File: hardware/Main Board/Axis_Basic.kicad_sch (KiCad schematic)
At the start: 58 parts, among them J1 USB_C_Receptacle_USB2.0, J2 JST_PH, J3 JST_PH, J4 S2B-PH-K-S, J5 1175-1628-ND, J6 1-84952-4, SW1 RKB2SJK, SW2 RKB2SJK, U1 TLV493D, U2 UA78M33CDCYR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

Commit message: PCB ordered
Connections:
- net AUX1: now reaches J6.5 (Pin_5)
- net AUX1: now also U3.15 (PA10/SERCOM0_2/SERCOM2_2)
- net AUX2: now reaches J6.6 (Pin_6)
- net AUX2: now also U3.28 (PA19/SERCOM1_3/SERCOM3_3)
- no-connect marks 11 -> 10
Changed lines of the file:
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@@
   (no_connect (at 40.64 54.61))
   (no_connect (at 139.7 39.37))
-  (no_connect (at 90.17 128.27))
   (no_connect (at 33.02 110.49))
   (no_connect (at 196.85 139.7))
@@
     )
   )
+  (global_label "AUX2" (shape input) (at 133.35 114.3 0) (fields_autoplaced)
+    (effects (font (size 1.27 1.27)) (justify left))
+    (property "Intersheetrefs" "${INTERSHEET_REFS}" (at 141.1733 114.3 0)
+      (effects (font (size 1.27 1.27)) (justify left) hide)
+    )
+  )
   (global_label "MOTOR_B2" (shape input) (at 237.49 121.92 0) (fields_autoplaced)
     (effects (font (size 1.27 1.27)) (justify left))
@@
     )
   )
+  (global_label "AUX2" (shape input) (at 63.5 115.57 0) (fields_autoplaced)
+    (effects (font (size 1.27 1.27)) (justify left))
+    (property "Intersheetrefs" "${INTERSHEET_REFS}" (at 71.3233 115.57 0)
+      (effects (font (size 1.27 1.27)) (justify left) hide)
+    )
+  )
   (global_label "EN" (shape input) (at 196.85 101.6 180) (fields_autoplaced)
     (effects (font (size 1.27 1.27)) (justify right))
@@
     )
   )
+  (global_label "AUX1" (shape input) (at 90.17 128.27 180) (fields_autoplaced)
+    (effects (font (size 1.27 1.27)) (justify right))
+    (property "Intersheetrefs" "${INTERSHEET_REFS}" (at 82.3467 128.27 0)
+      (effects (font (size 1.27 1.27)) (justify right) hide)
+    )
+  )
   (global_label "DIR" (shape input) (at 133.35 132.08 0) (fields_autoplaced)
     (effects (font (size 1.27 1.27)) (justify left))
@@
       (effects (font (size 1.27 1.27)) (justify left) hide)
     )
+  )
+  (global_label "AUX1" (shape input) (at 63.5 118.11 0) (fields_autoplaced)
+    (effects (font (size 1.27 1.27)) (justify left))
+    (property "Intersheetrefs" "${INTERSHEET_REFS}" (at 71.3233 118.11 0)
+      (effects (font (size 1.27 1.27)) (justify left) hide)
+    )

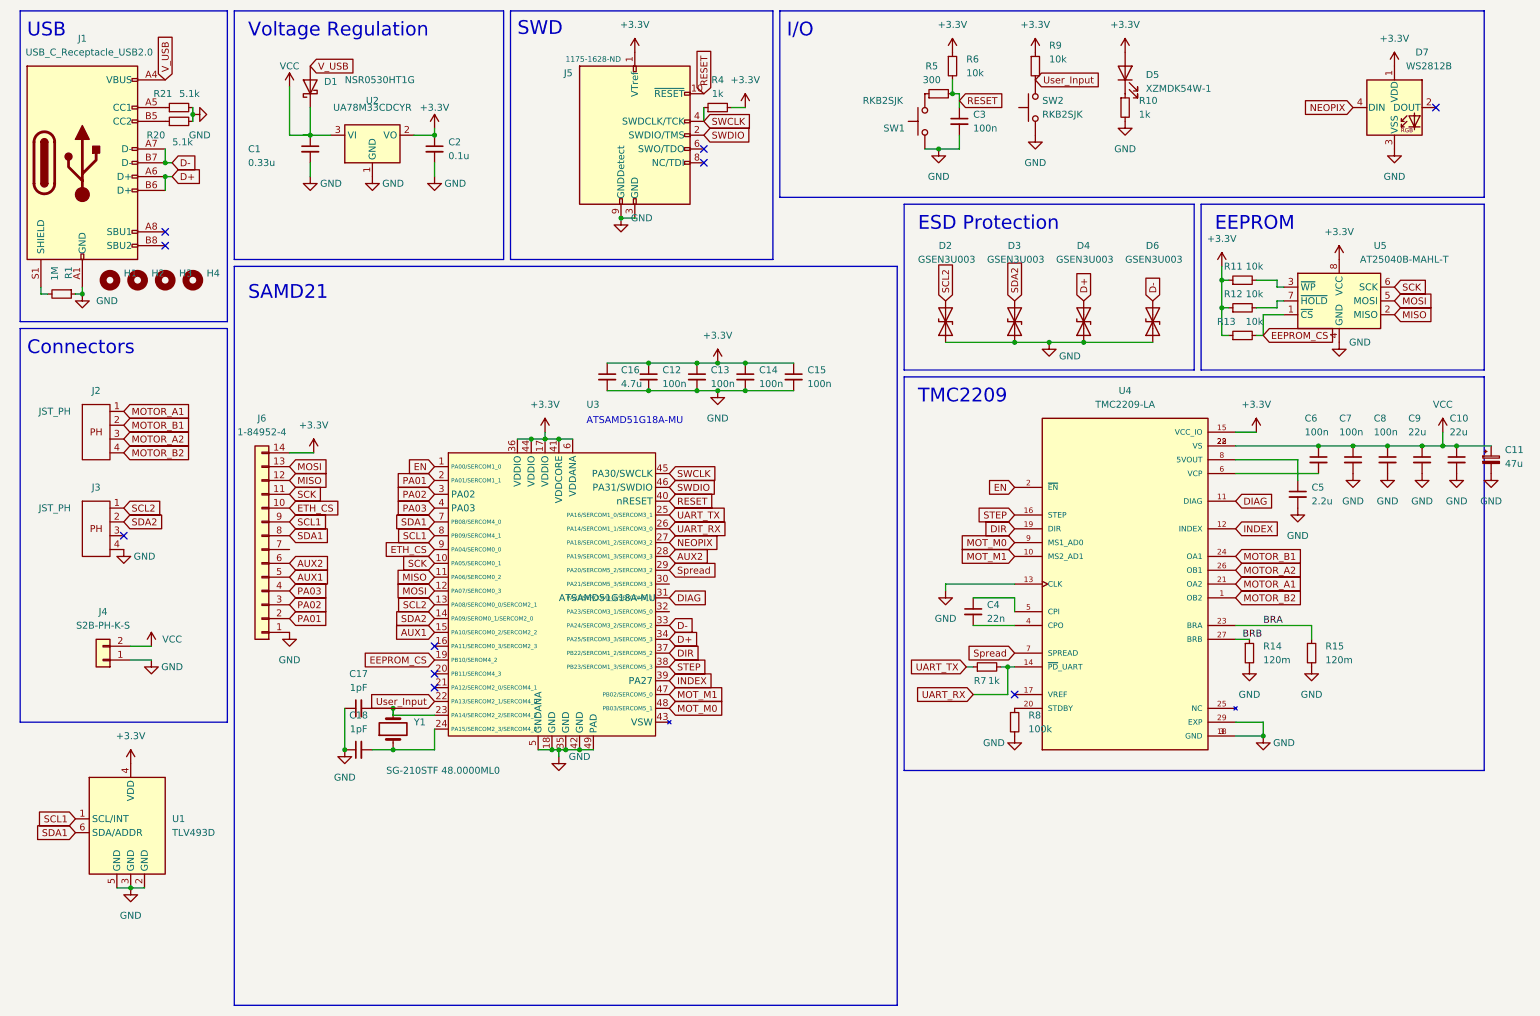
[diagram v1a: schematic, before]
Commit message: Add 32Mhz crystal
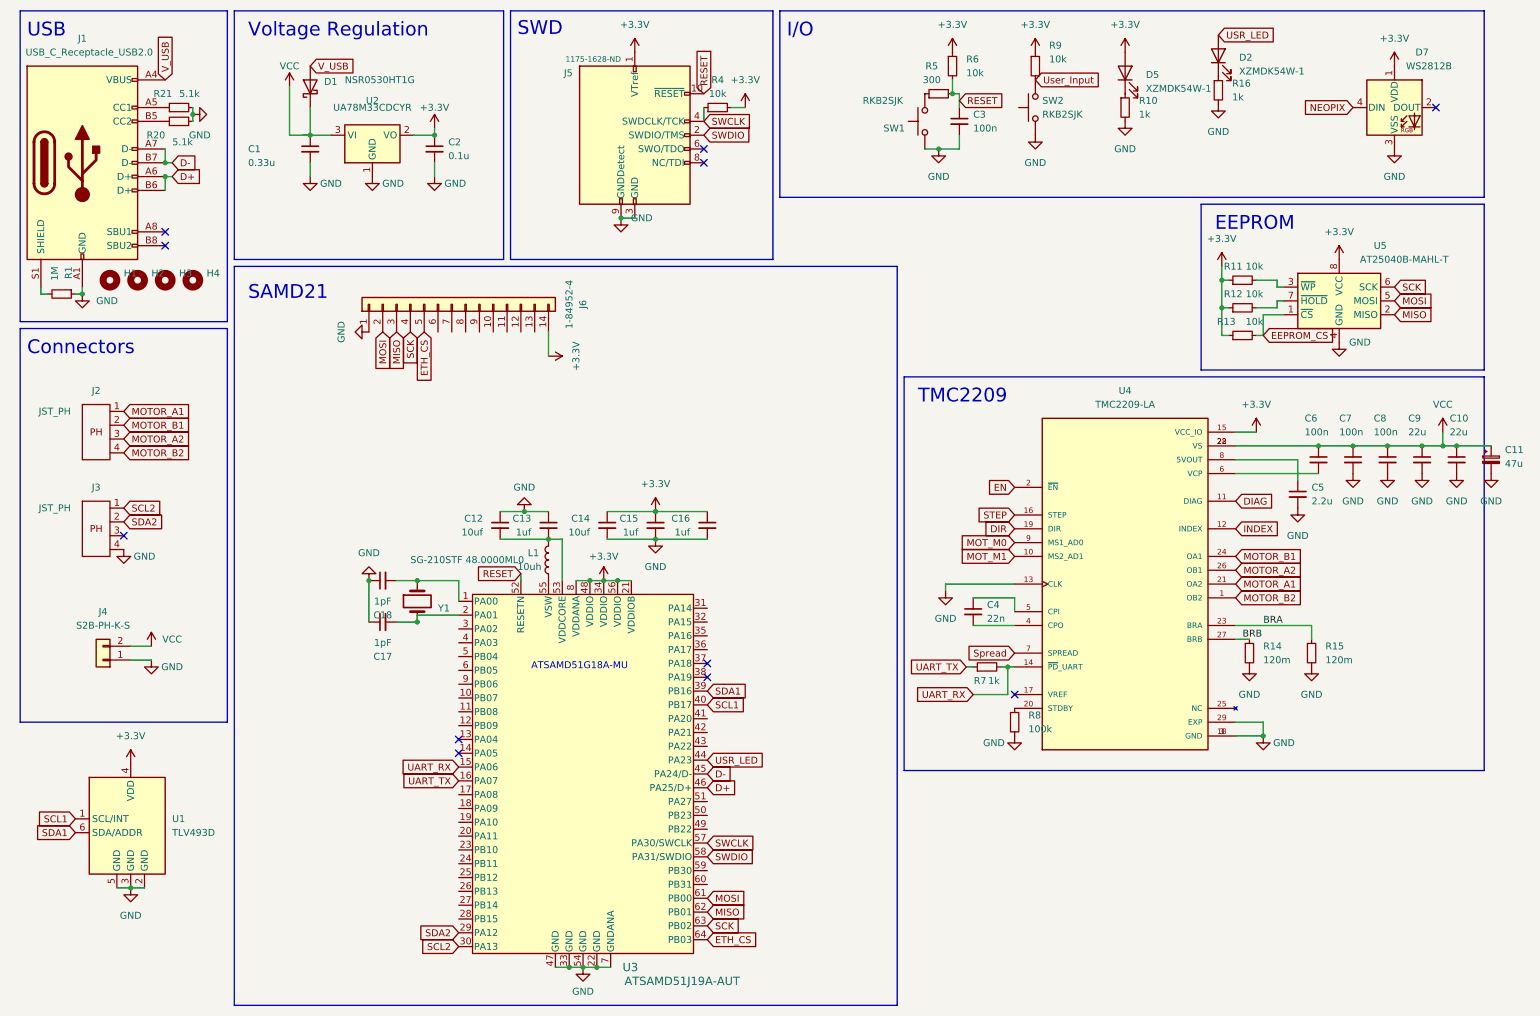
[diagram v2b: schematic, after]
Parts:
- removed D2, D3, D4, D6: GSEN3U003, Diode_SMD:D_0603_1608Metric, symbol Device:D_TVS
- removed U3: ATSAMD51G18A-MU, Package_DFN_QFN:VQFN-48-1EP_7x7mm_P0.5mm_EP5.15x5.15mm, symbol samd51G18:ATSAMD51G18A-MU
- added D2: XZMDK54W-1, LED_SMD:LED_0603_1608Metric, symbol Device:LED
- added L1: 10uh, Inductor_SMD:L_0603_1608Metric, symbol Device:L
- added R16: 1k, Resistor_SMD:R_0402_1005Metric, symbol Device:R_Small
- added U3: ATSAMD51J19A-AUT, Package_QFP:TQFP-64_10x10mm_P0.5mm, symbol ATSAMD51J19A-AUT:ATSAMD51J19A-AUT
- C12, C14: value 100n -> 10uf; footprint Capacitor_SMD:C_0402_1005Metric -> Capacitor_SMD:C_0805_2012Metric
- C13, C15: value 100n -> 1uf
- C16: value 4.7u -> 1uf
- J5: footprint Connector_PinHeader_1.27mm:PinHeader_2x05_P1.27mm_Horizontal -> JTAH:JTAG_Shielded
- R4: value 1k -> 10k
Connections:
- net AUX1 is gone; now on net ETH_CS: J6.5 (Pin_5)
- net PA01 is gone; now on net MOSI: J6.2 (Pin_2)
- net PA02 is gone; now on net MISO: J6.3 (Pin_3)
- net PA03 is gone; now on net SCK: J6.4 (Pin_4)
- net +3.3V: now also U3.21 (VDDIOB), U3.34 (VDDIO), U3.48 (VDDIO), U3.56 (VDDIO), U3.8 (VDDANA); no longer C12.1, C13.1
- net D+: now also U3.46 (PA25/D+)
- net D-: now also U3.45 (PA24/D-)
- net ETH_CS: now also U3.64 (PB03); no longer J6.10 (Pin_10)
- net GND: now also C12.1, C13.1, R16.2, U3.22 (GND), U3.33 (GND), U3.47 (GND), U3.54 (GND), U3.7 (GNDANA); no longer C12.2, C13.2
- net MISO: now also U3.62 (PB01); no longer J6.12 (Pin_12)
- net MOSI: now also U3.61 (PB00); no longer J6.13 (Pin_13)
- net RESET: now also U3.52 (RESETN)
- net SCK: now also U3.63 (PB02); no longer J6.11 (Pin_11)
- net SCL1: now also U3.40 (PB17); no longer J6.9 (Pin_9)
- net SCL2: now also U3.30 (PA13)
- net SDA1: now also U3.39 (PB16); no longer J6.8 (Pin_8)
- net SDA2: now also U3.29 (PA12)
- net SWCLK: now also U3.57 (PA30/SWCLK)
- net SWDIO: now also U3.58 (PA31/SWDIO)
- net UART_RX: now also U3.15 (PA06)
- net UART_TX: now also U3.16 (PA07)
- net at C18.2, Y1.1: now also U3.1 (PA00)
- net at C17.2, Y1.2: now also U3.2 (PA01)
- net AUX2: no longer names the net of J6.6 (Pin_6)
- new net: C12.2, C13.2, L1.2, U3.53 (VDDCORE)
- new net: D2.1 (K), R16.1
- new net: L1.1, U3.55 (VSW)
- new net USR_LED: D2.2 (A), U3.44 (PA23)
- no-connect marks 10 -> 11
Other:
- note removed: "ESD Protection"
- moved on the sheet: C17, C18, J6, Y1

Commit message: PCB V2 draft
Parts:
- added C19, C20: 1uf, Capacitor_SMD:C_0402_1005Metric, symbol Device:C_Small
- added R17, R18, R19, R20: 10k, Resistor_SMD:R_0402_1005Metric, symbol Device:R_Small
- C17, C18: value 1pF -> 22pF
- J1: value USB_C_Receptacle_USB2.0 -> USB4105-GF-A; footprint Connector_USB:USB_C_Receptacle_G-Switch_GT-USB-7010ASV -> Connector_USB:USB_C_Receptacle_GCT_USB4105-xx-A_16P_TopMnt_Horizontal
- Y1: value SG-210STF 48.0000ML0 -> 32.768; footprint Crystal:Crystal_SMD_2520-4Pin_2.5x2.0mm -> Crystal:Crystal_SMD_3215-2Pin_3.2x1.5mm
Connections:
- net +3.3V: now also C19.1, C20.1, R17.1, R18.1, R19.1, R20.1
- net DIAG: now also U3.18 (PA09)
- net DIR: now also U3.11 (PB08)
- net EEPROM_CS: now also U3.42 (PA21)
- net EN: now also U3.25 (PB12)
- net ETH_CS: now also J6.7 (Pin_7); no longer J6.5 (Pin_5)
- net GND: now also C19.2, C20.2
- net INDEX: now also U3.17 (PA08)
- net MISO: now also J6.5 (Pin_5); no longer J6.3 (Pin_3)
- net MOSI: now also J6.4 (Pin_4); no longer J6.2 (Pin_2)
- net MOT_M0: now also U3.20 (PA11)
- net MOT_M1: now also U3.19 (PA10)
- net NEOPIX: now also U3.10 (PB07)
- net SCK: now also J6.6 (Pin_6); no longer J6.4 (Pin_4)
- net SCL1: now also J6.12 (Pin_12), R20.2
- net SCL2: now also R17.2
- net SDA1: now also J6.13 (Pin_13), R19.2
- net SDA2: now also R18.2
- net STEP: now also U3.12 (PB09)
- net Spread: now also U3.24 (PB11)
- net USR_LED: now also U3.26 (PB13); no longer U3.44 (PA23)
- net PB04: now reaches J6.10 (Pin_10)
- net PB04: now also U3.5 (PB04)
- net PB05: now reaches J6.11 (Pin_11)
- net PB05: now also U3.6 (PB05)
- net PA02: now reaches J6.8 (Pin_8)
- net PA02: now also U3.3 (PA02)
- net PA03: now reaches J6.9 (Pin_9)
- net PA03: now also U3.4 (PA03)
- net SYNC: now reaches U3.31 (PA14)
- net SYNC: now also J3.3
- net PB30: now reaches U3.59 (PB30)
- net PB30: now also J6.2 (Pin_2)
- net PB31: now reaches U3.60 (PB31)
- net PB31: now also J6.3 (Pin_3)
- no-connect marks 11 -> 10
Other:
- note added: "ATSAMD51J19A-AUT"
- note removed: "ATSAMD51G18A-MU"
- moved on the sheet: C17, C18, Y1

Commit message: pcb ordered
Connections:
- no-connect marks 10 -> 22
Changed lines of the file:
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@@
   )
   (no_connect (at 40.64 54.61))
+  (no_connect (at 94.615 168.275))
   (no_connect (at 140.335 136.525))
+  (no_connect (at 94.615 178.435))
   (no_connect (at 139.7 39.37))
+  (no_connect (at 94.615 137.795))
+  (no_connect (at 140.335 151.765))
+  (no_connect (at 140.335 126.365))
+  (no_connect (at 94.615 180.975))
+  (no_connect (at 140.335 149.225))
   (no_connect (at 196.85 139.7))
+  (no_connect (at 140.335 161.925))
   (no_connect (at 94.615 150.495))
+  (no_connect (at 140.335 164.465))
   (no_connect (at 40.64 57.15))
+  (no_connect (at 140.335 159.385))
+  (no_connect (at 140.335 128.905))
   (no_connect (at 139.7 41.91))
+  (no_connect (at 140.335 131.445))
   (no_connect (at 140.335 133.985))
   (no_connect (at 94.615 147.955))
